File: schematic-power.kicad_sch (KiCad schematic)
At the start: 20 parts, among them U9 TPS62933

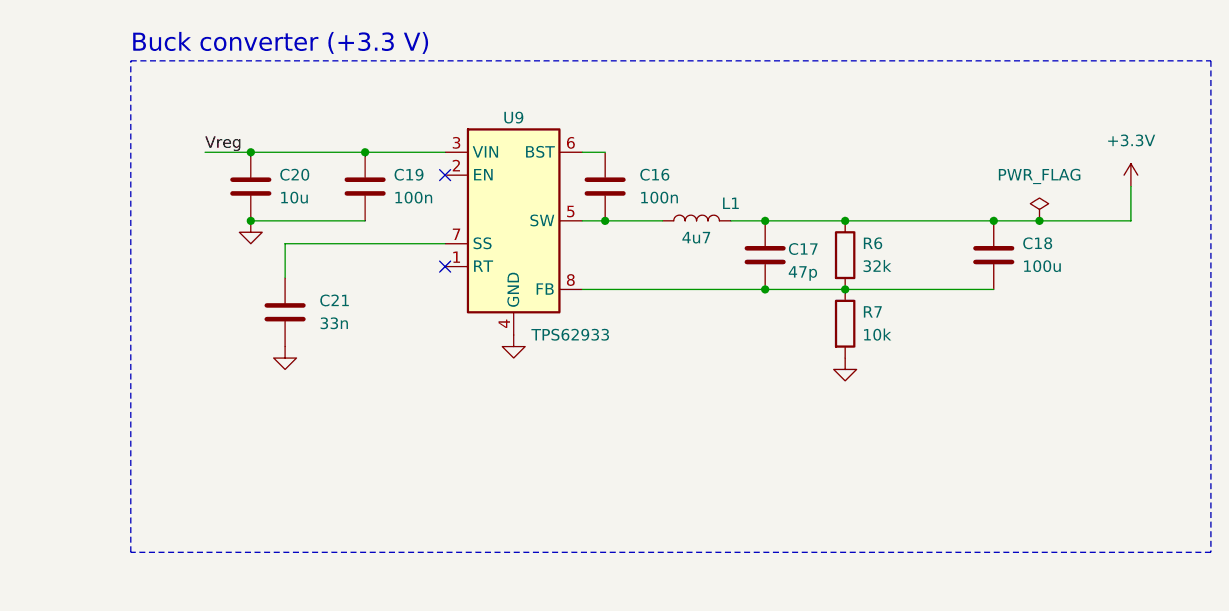
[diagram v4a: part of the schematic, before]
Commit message: Add Schottky Diode for VBUS and Vreg
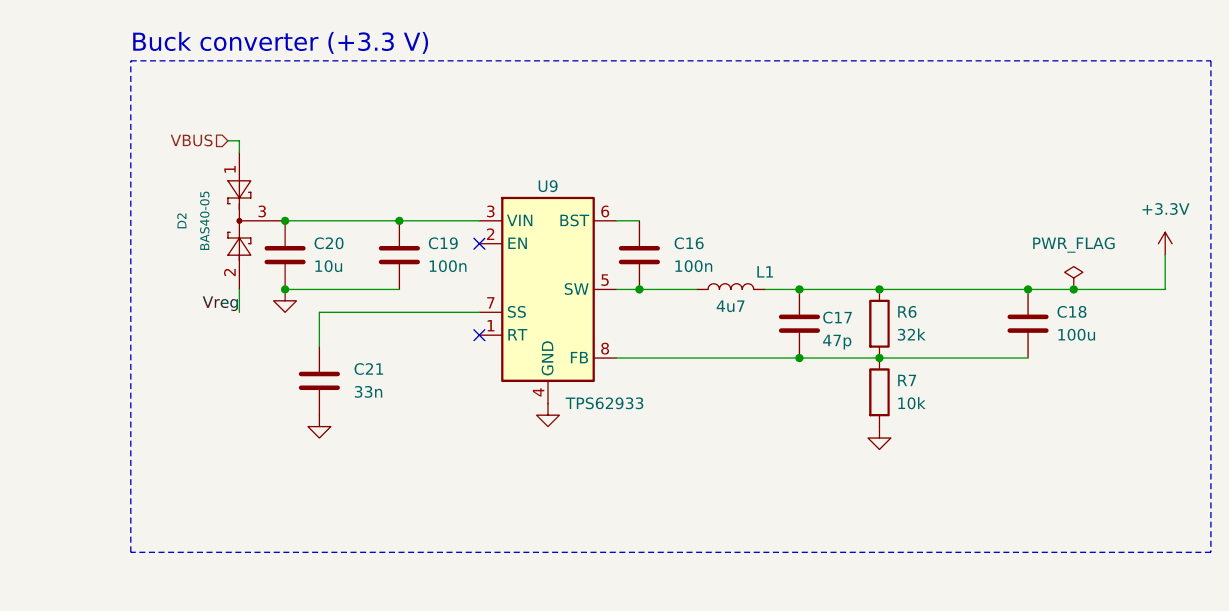
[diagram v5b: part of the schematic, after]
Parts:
- added D2: BAS40-05, Package_TO_SOT_SMD:SOT-23, symbol Diode:BAS40-04
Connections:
- net Vreg: now also D2.2; no longer C19.1, C20.1, U9.3 (VIN)
- new net: C19.1, C20.1, D2.3, U9.3 (VIN)
- new net VBUS: D2.1
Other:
- moved on the sheet: C16, C17, C18, C19, C20, C21, L1, R6, R7, U9

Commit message: PCB Drawing
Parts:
- C10: footprint (none) -> Capacitor_Tantalum_SMD:EEE0JA331XP
- C11, C16, C17, C18, C19, C20, C21, C9: footprint (none) -> Capacitor_SMD:C_1206_3216Metric
- D1: footprint Diode_SMD_AKL:D_SMC_TVS -> Diode_SMD:DIONM5436X244N
- L1: footprint (none) -> Inductor_SMD:SRN3015TA4R7M
- R10, R11, R12, R13, R6, R7, R9: footprint (none) -> Resistor_SMD:R_1206_3216Metric
- U?: footprint (none) -> Diode_SMD:SOP65P640X120-17N
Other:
- note added: "Removes the error"
- moved on the sheet: D1
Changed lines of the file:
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@@
   (junction (at 163.83 76.2) (diameter 0) (color 0 0 0 0)
+  )
+  (junction (at 179.07 68.58) (diameter 0) (color 0 0 0 0)
   )
   (junction (at 81.28 86.36) (diameter 0) (color 0 0 0 0)
@@
     (stroke (width 0) (type default))
   )
-  (wire (pts (xy 176.53 68.58) (xy 185.42 68.58))
+  (wire (pts (xy 176.53 68.58) (xy 179.07 68.58))
     (stroke (width 0) (type default))
   )
@@
     (stroke (width 0) (type default))
   )
+  (wire (pts (xy 44.45 62.23) (xy 44.45 60.96))
+    (stroke (width 0) (type default))
+  )
   (wire (pts (xy 120.65 85.09) (xy 120.65 86.36))
     (stroke (width 0) (type default))
@@
     (stroke (width 0) (type default))
   )
+  (wire (pts (xy 179.07 68.58) (xy 185.42 68.58))
+    (stroke (width 0) (type default))
+  )
   (wire (pts (xy 66.04 68.58) (xy 66.04 69.85))
     (stroke (width 0) (type default))
@@
   )
   (wire (pts (xy 120.65 77.47) (xy 120.65 74.93))
+    (stroke (width 0) (type default))
+  )
+  (wire (pts (xy 44.45 72.39) (xy 44.45 71.12))
     (stroke (width 0) (type default))
   )
@@
     (effects (font (size 2 2)) (justify left bottom))
   )
+  (text "Removes the error" (at 172.72 62.23 0)
+    (effects (font (size 0.8 0.8)) (justify left bottom))
+  )
   (text "TODO:\n\nAdd values\nMAYBE OPAMP" (at 113.03 101.6 0)
     (effects (font (size 1.27 1.27)) (justify left bottom))
@@
       (effects (font (size 1.27 1.27)) (justify left))
     )
-    (property "Footprint" "" (at 204.1652 76.2 0)
+    (property "Footprint" "Capacitor_SMD:C_1206_3216Metric" (at 204.1652 76.2 0)
       (effects (font (size 1.27 1.27)) hide)
     )
@@
       (effects (font (size 1.27 1.27)) (justify left))
     )
-    (property "Footprint" "" (at 58.1152 68.58 0)
+    (property "Footprint" "Capacitor_SMD:C_1206_3216Metric" (at 58.1152 68.58 0)
       (effects (font (size 1.27 1.27)) hide)
     )
@@
       (effects (font (size 1.27 1.27)))
     )
-    (property "Footprint" "" (at 96.52 58.42 0)
+    (property "Footprint" "Diode_SMD:SOP65P640X120-17N" (at 96.52 58.42 0)
       (effects (font (size 1.27 1.27)) hide)
     )
@@
           (reference "U1") (unit 1)
         )
+        (path "/c9ad7189-d3b2-414a-9743-efd8e57cd755/f92f58ec-64e0-437c-bc00-8ae46a3b3054"
+          (reference "U1") (unit 1)
+        )
       )
     )
@@
       (effects (font (size 1.27 1.27)) (justify left))
     )
-    (property "Footprint" "" (at 73.3552 83.82 0)
+    (property "Footprint" "Capacitor_SMD:C_1206_3216Metric" (at 73.3552 83.82 0)
       (effects (font (size 1.27 1.27)) hide)
     )
@@
       (effects (font (size 1.27 1.27)))
     )
-    (property "Footprint" "" (at 213.36 76.2 0)
+    (property "Footprint" "Inductor_SMD:SRN3015TA4R7M" (at 213.36 76.2 0)
       (effects (font (size 1.27 1.27)) hide)
     )
@@
       (effects (font (size 1.27 1.27)) (justify left))
     )
-    (property "Footprint" "" (at 228.092 80.01 90)
+    (property "Footprint" "Resistor_SMD:R_1206_3216Metric" (at 228.092 80.01 90)
       (effects (font (size 1.27 1.27)) hide)
     )
@@
       (effects (font (size 1.27 1.27)) (justify left))
     )
-    (property "Footprint" "" (at 106.172 64.77 90)
+    (property "Footprint" "Resistor_SMD:R_1206_3216Metric" (at 106.172 64.77 90)
       (effects (font (size 1.27 1.27)) hide)
     )
@@
       (effects (font (size 1.27 1.27)) (justify left))
     )
-    (property "Footprint" "" (at 221.9452 83.82 0)
+    (property "Footprint" "Capacitor_SMD:C_1206_3216Metric" (at 221.9452 83.82 0)
       (effects (font (size 1.27 1.27)) hide)
     )
@@
       (effects (font (size 1.27 1.27)) (justify left))
     )
-    (property "Footprint" "" (at 119.0752 69.85 0)
+    (property "Footprint" "Capacitor_Tantalum_SMD:EEE0JA331XP" (at 119.0752 69.85 0)
       (effects (font (size 1.27 1.27)) hide)
     )
@@
       (effects (font (size 1.27 1.27)) (justify left))
     )
-    (property "Footprint" "" (at 118.872 81.28 90)
+    (property "Footprint" "Resistor_SMD:R_1206_3216Metric" (at 118.872 81.28 90)
       (effects (font (size 1.27 1.27)) hide)
     )
@@
     )
   )
-  (symbol (lib_id "PCM_Diode_TVS_AKL:TPSMC30CA") (at 44.45 66.04 90) (unit 1)
-    (in_bom yes) (on_board yes) (dnp no) (fields_autoplaced)
-    (property "Reference" "D1" (at 47.625 64.7699 90)
+  (symbol (lib_id "PCM_Diode_TVS_AKL:TPSMC30CA") (at 44.45 67.31 90) (unit 1)
+    (in_bom yes) (on_board yes) (dnp no)
+    (property "Reference" "D1" (at 36.83 66.04 90)
       (effects (font (size 1.27 1.27)) (justify right))
     )
-    (property "Value" "TPSMC30CA" (at 47.625 67.3099 90)
-      (effects (font (size 1.27 1.27)) (justify right) hide)
-    )
-    (property "Footprint" "Diode_SMD_AKL:D_SMC_TVS" (at 44.45 66.04 0)
-      (effects (font (size 1.27 1.27)) hide)
-    )
-    (property "Datasheet" "https://www.tme.eu/Document/fe696fca10a75ca6fef9faefe21b9450/TPSMC_ser.pdf" (at 44.45 66.04 0)
+    (property "Value" "TPSMC30CA" (at 34.29 68.58 90)
+      (effects (font (size 1 1)) (justify right))
+    )
+    (property "Footprint" "Diode_SMD:DIONM5436X244N" (at 44.45 67.31 0)
+      (effects (font (size 1.27 1.27)) hide)
+    )
+    (property "Datasheet" "https://www.tme.eu/Document/fe696fca10a75ca6fef9faefe21b9450/TPSMC_ser.pdf" (at 44.45 67.31 0)
       (effects (font (size 1.27 1.27)) hide)
     )
@@
       (effects (font (size 1.27 1.27)) (justify left))
     )
-    (property "Footprint" "" (at 164.7952 76.2 0)
+    (property "Footprint" "Capacitor_SMD:C_1206_3216Metric" (at 164.7952 76.2 0)
       (effects (font (size 1.27 1.27)) hide)
     )
@@
       (effects (font (size 1.27 1.27)) (justify left))
     )
-    (property "Footprint" "" (at 64.262 64.77 90)
+    (property "Footprint" "Resistor_SMD:R_1206_3216Metric" (at 64.262 64.77 90)
       (effects (font (size 1.27 1.27)) hide)
     )
@@
       (effects (font (size 1.27 1.27)) (justify left))
     )
-    (property "Footprint" "" (at 247.3452 83.82 0)
+    (property "Footprint" "Capacitor_SMD:C_1206_3216Metric" (at 247.3452 83.82 0)
       (effects (font (size 1.27 1.27)) hide)
     )
@@
       (effects (font (size 1.27 1.27)) (justify left))
     )
-    (property "Footprint" "" (at 177.4952 76.2 0)
+    (property "Footprint" "Capacitor_SMD:C_1206_3216Metric" (at 177.4952 76.2 0)
       (effects (font (size 1.27 1.27)) hide)
     )
@@
       (effects (font (size 1.27 1.27)) (justify left))
     )
-    (property "Footprint" "" (at 168.6052 90.17 0)
+    (property "Footprint" "Capacitor_SMD:C_1206_3216Metric" (at 168.6052 90.17 0)
       (effects (font (size 1.27 1.27)) hide)
     )
@@
       (effects (font (size 1.27 1.27)) (justify left))
     )
-    (property "Footprint" "" (at 64.262 74.93 90)
+    (property "Footprint" "Resistor_SMD:R_1206_3216Metric" (at 64.262 74.93 90)
       (effects (font (size 1.27 1.27)) hide)
     )
@@
       (effects (font (size 1.27 1.27)) (justify left))
     )
-    (property "Footprint" "" (at 109.982 81.28 90)
+    (property "Footprint" "Resistor_SMD:R_1206_3216Metric" (at 109.982 81.28 90)
       (effects (font (size 1.27 1.27)) hide)
     )
@@
       (effects (font (size 1.27 1.27)) (justify left))
     )
-    (property "Footprint" "" (at 228.092 87.63 90)
+    (property "Footprint" "Resistor_SMD:R_1206_3216Metric" (at 228.092 87.63 90)
       (effects (font (size 1.27 1.27)) hide)
     )
@@
         )
       )
+    )
+  )
+  (symbol (lib_id "power:PWR_FLAG") (at 179.07 68.58 0) (unit 1)
+    (in_bom yes) (on_board yes) (dnp no) (fields_autoplaced)
+    (property "Reference" "#FLG05" (at 179.07 66.675 0)
+      (effects (font (size 1.27 1.27)) hide)
+    )
+    (property "Value" "PWR_FLAG" (at 179.07 63.5 0)
+      (effects (font (size 1.27 1.27)))
+    )
+    (property "Footprint" "" (at 179.07 68.58 0)
+      (effects (font (size 1.27 1.27)) hide)
+    )
+    (property "Datasheet" "~" (at 179.07 68.58 0)
+      (effects (font (size 1.27 1.27)) hide)
+    )
+    (pin "1")
+    (instances
+      (project "schematic-main"
+        (path "/c9ad7189-d3b2-414a-9743-efd8e57cd755/ed70203f-44bf-4bdc-8b45-a710eb8fc309"
+          (reference "#FLG05") (unit 1)
+        )
+      )

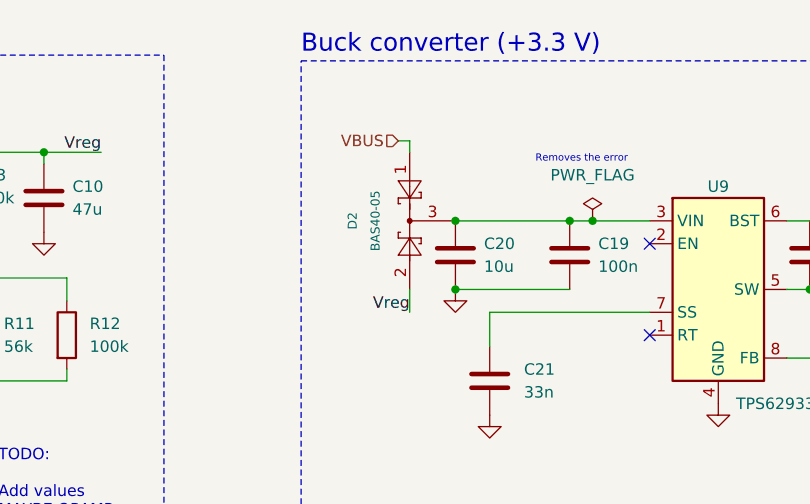
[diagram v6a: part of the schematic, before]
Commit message: Add Molex, change of layout for CAN and Optocouplers
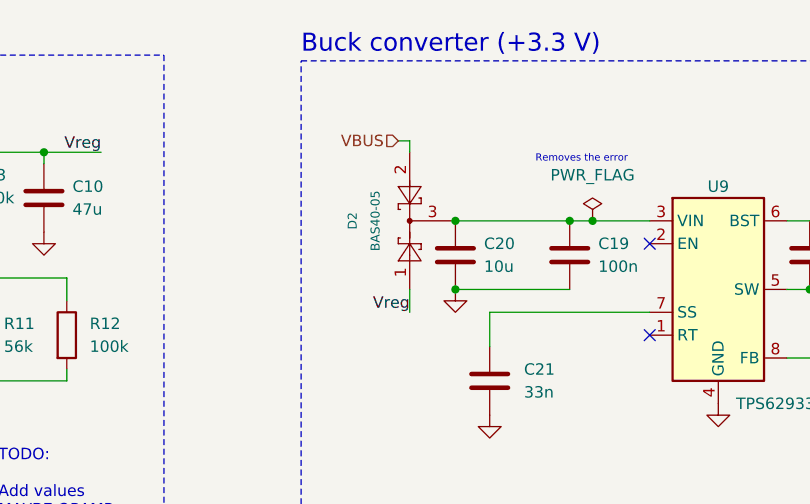
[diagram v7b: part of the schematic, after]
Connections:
- net VBUS: now also D2.2; no longer D2.1
- net Vreg: now also D2.1; no longer D2.2
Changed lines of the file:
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@@
     )
   )
-  (symbol (lib_id "Diode:BAS40-04") (at 161.29 68.58 90) (mirror x) (unit 1)
+  (symbol (lib_id "Diode:BAS40-04") (at 161.29 68.58 90) (unit 1)
     (in_bom yes) (on_board yes) (dnp no)
     (property "Reference" "D2" (at 152.4 68.58 0)
@@
       (effects (font (size 1 1)))
     )
-    (property "Footprint" "Package_TO_SOT_SMD:SOT-23" (at 153.67 62.23 0)
+    (property "Footprint" "Package_TO_SOT_SMD:SOT-23" (at 153.67 74.93 0)
       (effects (font (size 1.27 1.27)) (justify left) hide)
     )
-    (property "Datasheet" "http://www.vishay.com/docs/85701/bas40v.pdf" (at 153.67 66.04 0)
+    (property "Datasheet" "http://www.vishay.com/docs/85701/bas40v.pdf" (at 153.67 71.12 0)
       (effects (font (size 1.27 1.27)) hide)
     )

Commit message: Changing footprints for capacitors C >= 10 uF
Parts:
- C18, C20: footprint Capacitor_SMD:C_1206_3216Metric -> Capacitor_Tantalum_SMD:EEHZT1E331UP
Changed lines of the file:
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@@
       (effects (font (size 1.27 1.27)) (justify left))
     )
-    (property "Footprint" "Capacitor_SMD:C_1206_3216Metric" (at 164.7952 76.2 0)
+    (property "Footprint" "Capacitor_Tantalum_SMD:EEHZT1E331UP" (at 164.7952 76.2 0)
       (effects (font (size 1.27 1.27)) hide)
     )
@@
       (effects (font (size 1.27 1.27)) (justify left))
     )
-    (property "Footprint" "Capacitor_SMD:C_1206_3216Metric" (at 247.3452 83.82 0)
+    (property "Footprint" "Capacitor_Tantalum_SMD:EEHZT1E331UP" (at 247.3452 83.82 0)
       (effects (font (size 1.27 1.27)) hide)
     )
